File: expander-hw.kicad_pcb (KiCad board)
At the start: 2 copper layers, 46.5 x 35 mm, 67 parts, among them J1 USB_C_Receptacle_USB2.0_16P, J2 Conn_ARM_JTAG_SWD_10, J3 Conn_02x03_Odd_Even, J4 Conn_02x08_Odd_Even, U1 AZ1117-3.3, U10 MCP1501-10xCH, U2 TPS65130RGE, U3 USBLC6-2SC6, U4 STM32H523RETx, U5 SRDA3.3-4BTG, U6 SRDA3.3-4BTG, U7 SRDA3.3-4BTG, U8 DAC8562, U9 OPA2994xD

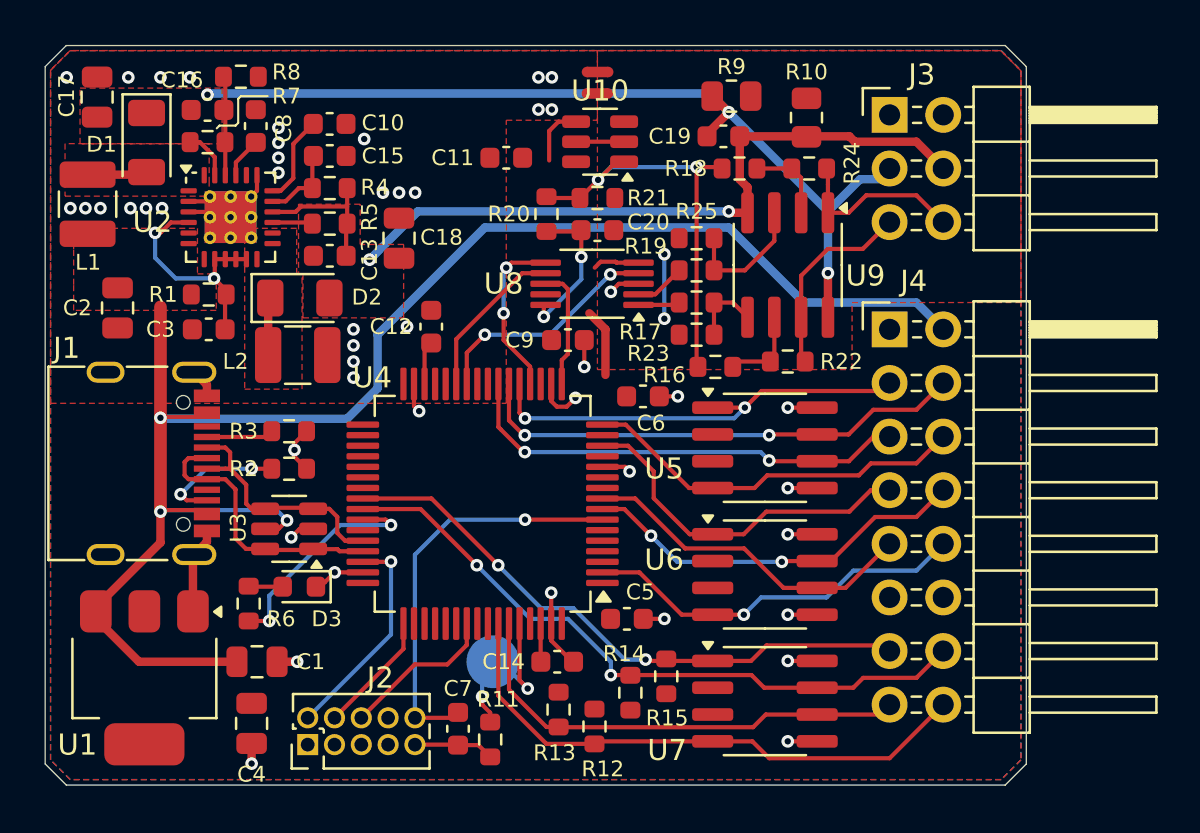
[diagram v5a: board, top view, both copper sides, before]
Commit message: Fix converter EMI
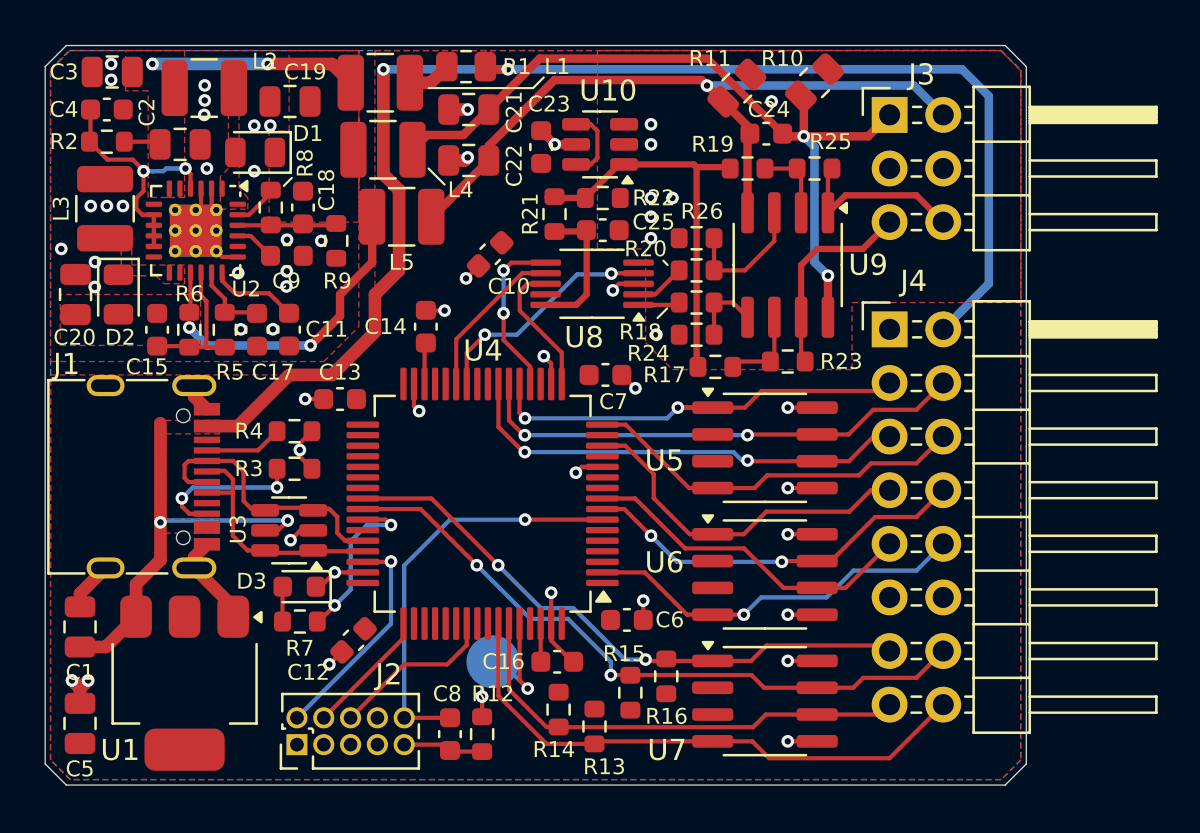
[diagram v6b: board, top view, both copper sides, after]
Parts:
- removed NT1, NT2: NetTie_2, NetTie:NetTie-2_SMD_Pad0.5mm
- added C12: 100nF, Capacitor_SMD:C_0603_1608Metric, F.Cu at (122.7, 105.9)
- added C13: 100nF, Capacitor_SMD:C_0603_1608Metric, F.Cu at (122.0, 94.5)
- added C21: 22uF, Capacitor_SMD:C_0805_2012Metric, F.Cu at (128.1, 80.8)
- added C22: 22uF, Capacitor_SMD:C_0805_2012Metric, F.Cu at (128.1, 83.2)
- added C3: 22uF, Capacitor_SMD:C_0805_2012Metric, F.Cu at (111.3, 79.0)
- added L1: 100uH, Inductor_SMD:L_1210_3225Metric, F.Cu at (124.0, 79.5)
- added L4: 4.7uH, Inductor_SMD:L_1210_3225Metric, F.Cu at (124.1, 82.7)
- added L5: 4.7uH, Inductor_SMD:L_1210_3225Metric, F.Cu at (125.0, 85.9)
- added R1: 10, Resistor_SMD:R_0805_2012Metric, F.Cu at (128.0, 78.7)
- C2: value 10uF -> 22uF
- D1, D2: footprint Diode_SMD:D_1206_3216Metric -> Diode_SMD:D_0805_2012Metric
- moved C20 15.6 mm to (109.5, 89.5)
- moved C4 11.5 mm to (111.0, 80.8), turned to 0 degrees
- moved L3 11.5 mm to (110.9, 85.5), turned to 90 degrees
- moved C11 9.94 mm to (119.6, 91.2), turned to -90 degrees
- moved C19 9.14 mm to (119.7, 80.4), turned to 180 degrees
- moved R9 8.99 mm to (121.9, 87.0), turned to 90 degrees
- moved C17 8.93 mm to (118.1, 91.2), turned to -90 degrees
- moved C15 8.90 mm to (113.4, 91.2), turned to 90 degrees
- moved R2 8.70 mm to (111.0, 82.3), turned to 0 degrees
- moved D2 8.60 mm to (111.5, 89.5), turned to -90 degrees
- moved C1 8.55 mm to (109.7, 105.3), turned to 90 degrees
- moved R5 8.35 mm to (116.6, 91.2), turned to 90 degrees
- moved R6 8.34 mm to (114.9, 91.2), turned to -90 degrees
- moved C2 8.29 mm to (114.5, 82.4), turned to 0 degrees
- moved C5 8.13 mm to (109.7, 109.9), turned to 90 degrees
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- renumbered C9 to C10, C10 to C11, C12 to C14, C13 to C15, C14 to C16, C15 to C17, C16 to C18, C17 to C19, C18 to C20, C11 to C23, C19 to C24, C20 to C25, C3 to C4, C4 to C5, C5 to C6, C6 to C7, C7 to C8, C8 to C9, L1 to L2, L2 to L3, R9 to R10, R10 to R11, R11 to R12, R12 to R13, R13 to R14, R14 to R15, R15 to R16, R16 to R17, R17 to R18, R18 to R19, R1 to R2, R19 to R20, R20 to R21, R21 to R22, R22 to R23, R23 to R24, R24 to R25, R25 to R26, R2 to R3, R3 to R4, R4 to R5, R5 to R6, R6 to R7, R7 to R8, R8 to R9
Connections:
- C15 pad 2: -12V -> Vneg
- C18 pad 1: +12V -> Vpos
- C19 pad 1: +12V -> Vpos
- C2 pad 1: VBUS -> PwrTps
- C20 pad 1: -12V -> Vneg
- C25 pad 2: GNDA -> GND
- D1 pad 1: +12V -> Vpos
- D2 pad 2: -12V -> Vneg
- J3 pad 1: GNDA -> +12V
- J3 pad 2: GNDA -> -12V
- J3 pad 3: +12V -> GND
- J3 pad 4: -12V -> GND
- L2 pad 1: VBUS -> PwrTps
- R10 pad 1: GNDA -> GND
- R11 pad 1: GNDA -> GND
- R2 pad 2: VBUS -> PwrTps
- R22 pad 1: GNDA -> GND
- R24 pad 1: GNDA -> GND
- R26 pad 1: GNDA -> GND
- R6 pad 1: -12V -> Vneg
- R8 pad 2: +12V -> Vpos
- U10 pad 2: GNDA -> GND
- U10 pad 3: GNDA -> GND
- U10 pad 5: GNDA -> GND
- U2 pad 15: -12V -> Vneg
- U2 pad 23: +12V -> Vpos
- U2 pad 5: VBUS -> PwrTps
- U2 pad 6: VBUS -> PwrTps
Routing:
- net Vneg: track 0.00 -> 15.4 mm, vias 0 -> 2
- net PwrTps: track 0.00 -> 11.3 mm, vias 0 -> 2
- net +12V: track 45.5 -> 37.3 mm, vias 3 -> 2
- net VBUS: track 79.4 -> 86.7 mm, vias 3 -> 4
- net GND: track 43.5 -> 50.3 mm, vias 46 -> 55
- net GNDA: track 5.33 -> 0.00 mm, vias 2 -> 0
- net +3.3V: track 8.30 -> 3.55 mm
- net CoilPos: track 2.81 -> 0.00 mm
- net CoilNeg: track 2.74 -> 0.00 mm
- net /LED_HRTB: track 10.8 -> 8.17 mm
- net Vpos: track 0.00 -> 2.13 mm
- net Net-(L1-Pad1): track 0.00 -> 2.07 mm
- net /D-: track 11.8 -> 13.2 mm
- net Net-(U2-ENN): track 11.3 -> 12.5 mm
- net /D+: track 13.1 -> 11.9 mm
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- added copper zone on F.Cu, net PwrTps
- added copper zone on F.Cu, net Vneg
- added copper zone on F.Cu, net Vpos
- removed copper zone on F.Cu, net +12V
- removed copper zone on F.Cu, net -12V
- removed copper zone on F.Cu, net GNDA

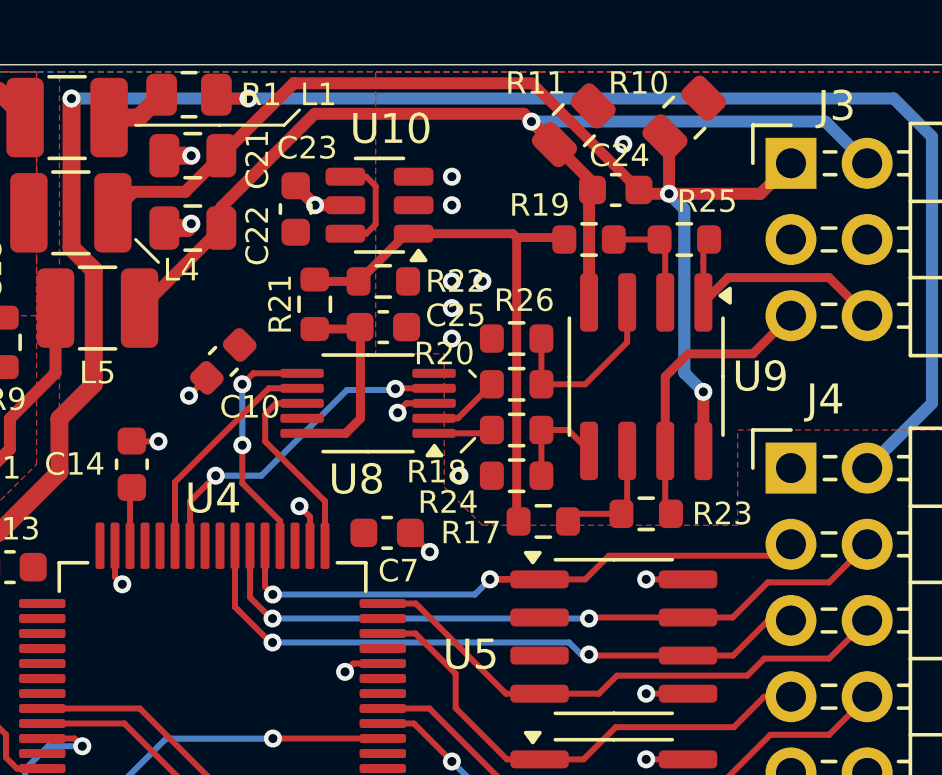
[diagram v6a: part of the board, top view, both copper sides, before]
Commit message: Remove Vref divider
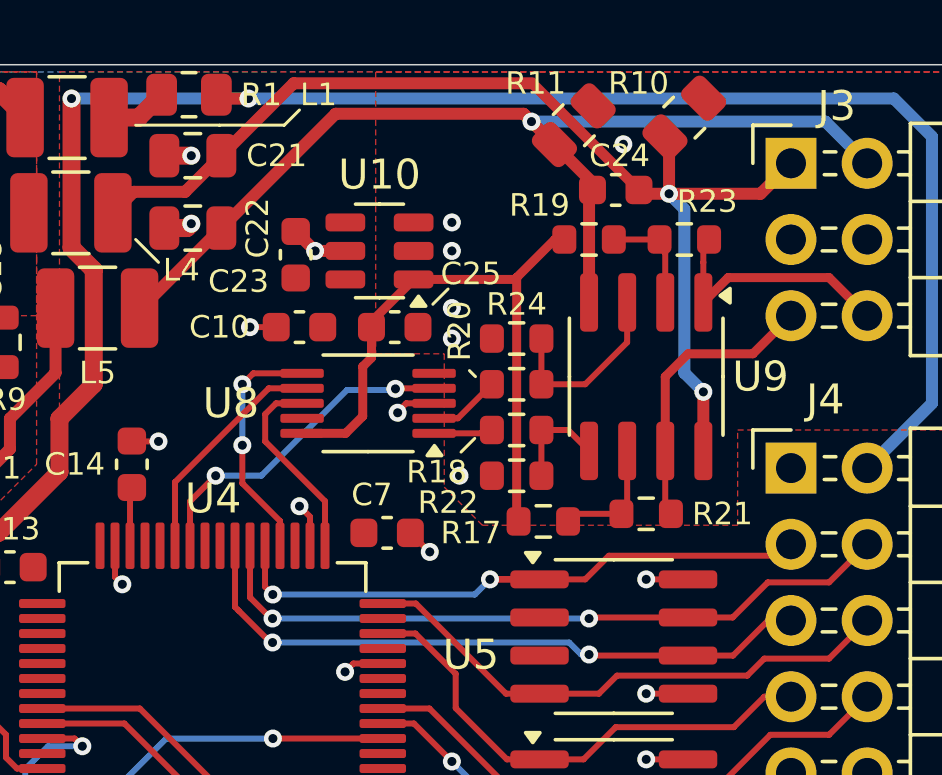
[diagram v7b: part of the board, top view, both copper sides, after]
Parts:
- removed the R21 at (132.2, 85.7)
- removed the R22 at (134.5, 85.0)
- moved C10 2.79 mm to (131.7, 86.5), turned to 180 degrees
- moved C23 1.52 mm to (131.6, 84.1)
- moved U10 1.52 mm to (134.4, 83.9)
- moved C25 0.38 mm to (134.9, 86.5)
- renumbered R23 to R21, R24 to R22, R25 to R23, R26 to R24
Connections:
- C25 pad 1: Net-(U8-V_{REF}IN/OUT) -> Net-(U10-OUT)
- U8 pad 10: Net-(U8-V_{REF}IN/OUT) -> Net-(U10-OUT)
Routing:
- net Net-(U8-V_{REF}IN/OUT): track 6.59 -> 0.00 mm
- net +3.3V: track 3.55 -> 0.00 mm
- net Net-(U10-OUT): track 19.0 -> 21.7 mm
- net GND: track 50.3 -> 50.1 mm, vias 55 -> 53
